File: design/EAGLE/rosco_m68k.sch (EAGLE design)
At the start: 57 parts, among them IC1 74LS04N, IC10 74LS32N, IC11 NE555N, IC12 74LS01N, IC2 MC68010P10, IC3 ATF16V8QL-15PU, IC4 74LS93N, IC5 74S20N, IC6 MC68901P, IC7 74LS08N, IC8 74LS08N, IC9 74LS174N, Q1 1.8432MHz, Q2 8MHz, U1 AT28C64B-15PU, U2 AT28C64B-15PU, U3 AS6C4008-55PCN, U4 AS6C4008-55PCN

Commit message: Cleanup ready for PCB design
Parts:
- added C16, C20, C21, C22, C23, C25, C27, C29: 100nF, capacitor-wima:C2,5-3
- added C17, C18, C19, C28, C30: 100uF, rcl:CPOL-EUE2.5-5
- added C24, C26: 22pF, capacitor-wima:C2,5-3
- added C31: 400uF, rcl:CPOL-EUE3.5-10
- added JP2: PWR, pinhead:PINHD-1X2
- C1, C2: device capacitor-wima:C2.5/2 -> capacitor-wima:C2,5-3
- C10, C7, C8, C9: device capacitor-wima:C5/3 -> capacitor-wima:C2,5-3
- C11: value 22pF -> 33pF; device rcl:C-EU025-025X050 -> capacitor-wima:C2,5-3
- C12: value 100nF -> 33pF; device rcl:C-EU025-025X050 -> capacitor-wima:C2,5-3
- C13: value 22pF -> 100nF; device rcl:C-EU025-025X050 -> capacitor-wima:C2,5-3
- C14: value 100uF -> 100nF; device rcl:CPOL-EUE1.8-4 -> capacitor-wima:C2,5-3
- C3: value 33pF -> 100uF; device capacitor-wima:C2,5-3 -> rcl:CPOL-EUE2.5-5
- C4: value 33pF -> 100nF
- C5: value 100nF -> 100uF; device capacitor-wima:C2,5-3 -> rcl:CPOL-EUE2.5-5
- R1, R10, R11, R12, R5, R6, R7, R8, R9: device rcl:R-US_0207/10 -> rcl:R-EU_0207/10
- R13, R14, R15, R16, R17, R18, R2, R3, R4: device rcl:R-US_0204/7 -> rcl:R-EU_0207/10
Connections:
- net GND: now also C12.2, C14.2, C15.2, C16.2, C17.-, C18.-, C19.-, C20.2, C21.2, C22.2, C23.2, C24.2, C26.2, C27.2, C28.-, C3.-, C30.-, C31.-, C5.-, IC12P.GND, IC1P.GND, IC4P.GND, IC5P.GND, IC8P.GND, JP2.2; no longer C14.-, C3.2, C5.2
- net N$19: now also C29.2; no longer C15.2
- net N$3: now also C25.1; no longer C12.1
- net N$37: now also C28.+; no longer C14.+
- net N$4: now also C25.2; no longer C12.2
- net N$5: now also C26.1; no longer C13.1
- net N$6: now also C24.1; no longer C11.1
- net N$7: now also C11.1; no longer C3.1
- net N$8: now also C12.1; no longer C4.1
- net VCC: now also C13.1, C14.1, C16.1, C17.+, C18.+, C19.+, C20.1, C21.1, C22.1, C23.1, C27.1, C29.1, C3.+, C30.+, C31.+, C4.1, C5.+, IC12P.VCC, IC1P.VCC, IC4P.VCC, IC5P.VCC, IC8P.VCC, JP2.1; no longer C5.1
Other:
- note added: "CLOCK & RESET"
- moved on the sheet: C1, C2, IC10P, IC7P, IC9P

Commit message: Use new PLD glue logic and tidy up
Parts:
- removed C29: 100nF, capacitor-wima:C2,5-3
- removed C30: 100uF, rcl:CPOL-EUE2.5-5
- removed C31: 400uF, rcl:CPOL-EUE3.5-10
- removed IC10: 74LS32N, 74xx-eu:74LS32N
- removed IC11: NE555N, linear:NE555N
- removed IC12: 74LS01N, 74xx-eu:74LS01N
- removed R18: 4K7, rcl:R-EU_0207/10
- added JP3: (no value), pinhead:PINHD-2X30
- added JP4: (no value), pinhead:PINHD-2X2
- C10: value 100nF -> 33pF
- C12: value 33pF -> 100nF
- C16, C2, C25, C27, C4: value 100nF -> 100uF; device capacitor-wima:C2,5-3 -> rcl:CPOL-EUE2.5-5
- C19, C3, C5: value 100uF -> 100nF; device rcl:CPOL-EUE2.5-5 -> capacitor-wima:C2,5-3
- C20, C22: value 100nF -> 22pF
- C24, C26: value 22pF -> 100nF
- C28: value 100uF -> 400uF; device rcl:CPOL-EUE2.5-5 -> rcl:CPOL-EUE3.5-10
- IC1: value 74LS04N -> MC68010P10; device 74xx-eu:74LS04N -> micro-mc68000:MC68000P
- IC2: value MC68010P10 -> ATF16V8QL-15PU; device micro-mc68000:MC68000P -> atmel:ATF16V8BP3; MPN (none) -> ATF16V8QL-15PU; PROG (none) -> ADDRESS_DECODER.PLD
- IC3: value ATF16V8QL-15PU -> 74LS93N; device atmel:ATF16V8BP3 -> 74xx-eu:74LS93N; MPN ATF16V8QL-15PU -> (none); PROG ADDRESS_DECODER.PLD -> (none)
- IC4: value 74LS93N -> MC68901P; device 74xx-eu:74LS93N -> micro-mc68000:MC68901P
- IC5: value 74S20N -> ATF16V8QL-15PU; device 74xx-eu:74S20N -> atmel:ATF16V8BP3; MPN (none) -> ATF16V8QL-15PU; PROG (none) -> GLUE_LOGIC.PLD
- IC6: value MC68901P -> 74LS174N; device micro-mc68000:MC68901P -> 74xx-eu:74LS174N
- IC7: value 74LS08N -> 74LS04N; device 74xx-eu:74LS08N -> 74xx-eu:74LS04N
- IC8: value 74LS08N -> NE555N; device 74xx-eu:74LS08N -> linear:NE555N
- IC9: value 74LS174N -> 74LS01N; device 74xx-eu:74LS174N -> 74xx-eu:74LS01N
- JP1: device pinhead:PINHD-1X3 -> pinhead:PINHD-1X4; 1 CP2102 TXD -> GND; 2 CP2102 RXD -> TXD; 3 CP2102 CTS -> RXD; 4 (none) -> CTS
- R10, R5: value 4K7 -> 1K2
- R11, R6: value 1K2 -> 4K7
- R12: value 4K7 -> 2K2
- R13: value 2K2 -> 270R
- R14: value 270R -> 330R
- R16: value 330R -> 4K7
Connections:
- removed net IACK: IC10B.I1, IC1E.O
- removed net N$11: IC6G$1.RC, IC6G$1.TC, IC6G$1.TDO
- removed net N$12: IC6G$1.I0, LED1.C
- removed net N$13: IC6G$1.SI, JP1.1
- removed net N$14: IC6G$1.SO, JP1.2
- removed net N$15: IC8B.O, IC8C.I0
- removed net N$17: IC6G$1.I1, LED2.C
- removed net N$18: IC6G$1.I7, JP1.3
- removed net N$2: IC2G$1.VPA, R1.1
- removed net N$24: IC8A.O, IC8C.I1
- removed net N$25: IC10B.I0, IC8C.O
- removed net N$27: IC10A.I0, IC8D.O
- removed net N$28: IC10B.O, IC7B.I0
- removed net N$29: IC10A.O, IC7B.I1
- removed net N$7: C11.1, IC6G$1.XTAL1, Q1.1
- removed net N$8: C12.1, IC6G$1.XTAL2, Q1.2
- new net MFPIO0: IC4G$1.I0, LED1.C
- new net MFPIO1: IC4G$1.I1, LED2.C
- new net MFPXTAL1: C10.1, IC4G$1.XTAL1, Q1.1
- new net MFPXTAL2: C11.1, IC4G$1.XTAL2, Q1.2
- new net UARTCLK: IC4G$1.RC, IC4G$1.TC, IC4G$1.TDO
- new net UARTCTS: IC4G$1.I7, JP1.4
- new net UARTRX: IC4G$1.SI, JP1.3
- new net UARTTX: IC4G$1.SO, JP1.2
- new net VPA: IC1G$1.VPA, R1.1
- net /BOOT: now also IC2.I8, IC6A.Q6; no longer IC3.I8, IC9A.Q6
- net /HALT: now also IC1G$1.HALT, IC9A.O, IC9C.I0, IC9C.I1, R16.1; no longer IC12A.O, IC12C.I0, IC12C.I1, IC2G$1.HALT, R17.1
- net /IACK: now also IC2.O2, IC4G$1.IACK, IC5.O7; no longer IC1E.I, IC3.O2, IC5A.O, IC6G$1.IACK, IC7A.I1, IC8D.I0
- net /IODTACK: now also IC4G$1.DTACK, IC5.I8; no longer IC10A.I1, IC6G$1.DTACK, R4.1
- net /MFPDS: now also IC4G$1.DS, IC5.O5; no longer IC6G$1.DS, IC7A.O
- net /RAMOE: now also IC5.O4; no longer IC1A.O
- net A1: now also IC1G$1.A1, IC4G$1.RS5, JP3.1; no longer IC2G$1.A1, IC6G$1.RS5
- net A10: now also IC1G$1.A10, JP3.19; no longer IC2G$1.A10
- net A11: now also IC1G$1.A11, JP3.21; no longer IC2G$1.A11
- net A12: now also IC1G$1.A12, JP3.23; no longer IC2G$1.A12
- net A13: now also IC1G$1.A13, JP3.25; no longer IC2G$1.A13
- net A14: now also IC1G$1.A14, JP3.27; no longer IC2G$1.A14
- net A15: now also IC1G$1.A15, JP3.29; no longer IC2G$1.A15
- net A16: now also IC1G$1.A16, JP3.31; no longer IC2G$1.A16
- net A17: now also IC1G$1.A17, JP3.33; no longer IC2G$1.A17
- net A18: now also IC1G$1.A18, IC2.CLK, JP3.35; no longer IC2G$1.A18, IC3.CLK
- net A19: now also IC1G$1.A19, IC2.I1, JP3.37; no longer IC2G$1.A19, IC3.I1
- net A2: now also IC1G$1.A2, IC4G$1.RS4, JP3.3; no longer IC2G$1.A2, IC6G$1.RS4
- net A20: now also IC1G$1.A20, IC2.I2, JP3.39; no longer IC2G$1.A20, IC3.I2
- net A21: now also IC1G$1.A21, IC2.I3, JP3.41; no longer IC2G$1.A21, IC3.I3
- net A22: now also IC1G$1.A22, IC2.I4, JP3.43; no longer IC2G$1.A22, IC3.I4
- net A23: now also IC1G$1.A23, IC2.I5, JP3.45; no longer IC2G$1.A23, IC3.I5
- net A3: now also IC1G$1.A3, IC4G$1.RS3, JP3.5; no longer IC2G$1.A3, IC6G$1.RS3
- net A4: now also IC1G$1.A4, IC4G$1.RS2, JP3.7; no longer IC2G$1.A4, IC6G$1.RS2
- net A5: now also IC1G$1.A5, IC4G$1.RS1, JP3.9; no longer IC2G$1.A5, IC6G$1.RS1
- net A6: now also IC1G$1.A6, JP3.11; no longer IC2G$1.A6
- net A7: now also IC1G$1.A7, JP3.13; no longer IC2G$1.A7
- net A8: now also IC1G$1.A8, JP3.15; no longer IC2G$1.A8
- net A9: now also IC1G$1.A9, JP3.17; no longer IC2G$1.A9
- net AS: now also IC1G$1.AS, IC2.OE, IC6A.CLK, JP3.47; no longer IC2G$1.AS, IC3.OE, IC9A.CLK
- net BERR: now also IC1G$1.BERR, JP3.49, R11.1; no longer IC2G$1.BERR, R12.1
- net BG: now also IC1G$1.BG, JP3.51; no longer IC2G$1.BG
- net BGACK: now also IC1G$1.BGACK, JP3.53, R9.1; no longer IC2G$1.BGACK, R10.1
- net BR: now also IC1G$1.BR, JP3.55, R8.1; no longer IC2G$1.BR, R9.1
- net CLK: now also IC1G$1.CLK, IC3A.CKA, IC7C.O, JP3.4; no longer IC1D.O, IC2G$1.CLK, IC4A.CKA
- net D0: now also IC1G$1.D0, IC4G$1.D0, JP4.1; no longer IC2G$1.D0, IC6G$1.D0
- net D1: now also IC1G$1.D1, IC4G$1.D1, JP4.3; no longer IC2G$1.D1, IC6G$1.D1
- net D10: now also IC1G$1.D10, JP3.48; no longer IC2G$1.D10
- net D11: now also IC1G$1.D11, JP3.46; no longer IC2G$1.D11
- net D12: now also IC1G$1.D12, JP3.44; no longer IC2G$1.D12
- net D13: now also IC1G$1.D13, JP3.42; no longer IC2G$1.D13
- net D14: now also IC1G$1.D14, JP3.40; no longer IC2G$1.D14
- net D15: now also IC1G$1.D15, JP3.38; no longer IC2G$1.D15
- net D2: now also IC1G$1.D2, IC4G$1.D2, JP4.4; no longer IC2G$1.D2, IC6G$1.D2
- net D3: now also IC1G$1.D3, IC4G$1.D3, JP4.2; no longer IC2G$1.D3, IC6G$1.D3
- net D4: now also IC1G$1.D4, IC4G$1.D4, JP3.60; no longer IC2G$1.D4, IC6G$1.D4
- net D5: now also IC1G$1.D5, IC4G$1.D5, JP3.58; no longer IC2G$1.D5, IC6G$1.D5
- net D6: now also IC1G$1.D6, IC4G$1.D6, JP3.56; no longer IC2G$1.D6, IC6G$1.D6
- net D7: now also IC1G$1.D7, IC4G$1.D7, JP3.54; no longer IC2G$1.D7, IC6G$1.D7
- net D8: now also IC1G$1.D8, JP3.52; no longer IC2G$1.D8
- net D9: now also IC1G$1.D9, JP3.50; no longer IC2G$1.D9
- net DTACK: now also IC1G$1.DTACK, IC5.O6, JP3.57; no longer IC2G$1.DTACK, IC7B.O
- net EVENRAMSEL: now also IC2.O8, IC5.I6, JP3.8; no longer IC3.O8, IC8A.I1
- net EVENROMSEL: now also IC2.O6, IC5.I5, JP3.10; no longer IC3.O6, IC8B.I1
- net EXPSEL: now also IC2.O3, JP3.18; no longer IC3.O3
- net FC0: now also IC1G$1.FC0, IC5.CLK, JP3.20; no longer IC2G$1.FC0, IC5A.I3
- net FC1: now also IC1G$1.FC1, IC5.I1, JP3.22; no longer IC2G$1.FC1, IC5A.I2
- net FC2: now also IC1G$1.FC2, IC5.I2, JP3.24; no longer IC2G$1.FC2, IC5A.I0, IC5A.I1
- net GND: now also C16.-, C19.2, C2.-, C25.-, C27.-, C3.2, C4.-, C5.2, IC1P.GND@1, IC1P.GND@2, IC2.GND, IC3A.CKB, IC3A.R0(1), IC3A.R0(2), IC3P.GND, IC4G$1.IEI, IC4G$1.TAI, IC4G$1.TBI, IC5.GND, IC5.OE, IC6A.D2, IC6A.D5, IC7D.I, IC7E.I, IC7F.I, IC8.GND, IC9D.I0, IC9D.I1, JP1.1, JP3.6, R13.1; no longer C16.2, C19.-, C2.2, C21.2, C26.2, C27.2, C3.-, C30.-, C31.-, C4.2, C5.-, IC10C.I0, IC10C.I1, IC10D.I0, IC10D.I1, IC10P.GND, IC11.GND, IC12D.I0, IC12D.I1, IC12P.GND, IC1F.I, IC1P.GND, IC2P.GND@1, IC2P.GND@2, IC3.GND, IC4A.CKB, IC4A.R0(1), IC4A.R0(2), IC5B.I0, IC5B.I1, IC5B.I2, IC5B.I3, IC5P.GND, IC6G$1.IEI, IC6G$1.TAI, IC6G$1.TBI, IC7C.I0, IC7C.I1, IC7D.I0, IC7D.I1, IC8P.GND, IC9A.D2, IC9A.D5, R15.1
- net IOSEL: now also IC2.O4, IC4G$1.CS, IC5.I7, JP3.16; no longer IC3.O4, IC6G$1.CS, IC8D.I1
- net IPL0: now also IC1G$1.IPL0, JP3.26, R7.1; no longer IC2G$1.IPL0, R8.1
- net IPL1: now also IC1G$1.IPL1, JP3.28, R6.1; no longer IC2G$1.IPL1, R7.1
- net IPL2: now also IC1G$1.IPL2, IC4G$1.IRQ, JP3.30, R4.1; no longer IC2G$1.IPL2, IC6G$1.IRQ, R5.1
- net LDS: now also IC1G$1.LDS, IC2.I7, IC5.O2, JP3.32; no longer IC2G$1.LDS, IC3.I7, IC7A.I0
- net MFPCLK: now also IC3A.QA, IC4G$1.CLK; no longer IC4A.QA, IC6G$1.CLK
- net N$16: now also IC6A.D4, IC6A.Q3; no longer IC9A.D4, IC9A.Q3
- net N$19: now also C26.2, IC8.CV; no longer C29.2, IC11.CV
- net N$20: now also R14.2; no longer R15.2
- net N$22: now also IC6A.D6, IC6A.Q4; no longer IC9A.D6, IC9A.Q4
- net N$23: now also IC6A.D3, IC6A.Q1; no longer IC9A.D3, IC9A.Q1
- net N$3: now also C21.1, IC7A.O, R5.2; no longer C25.1, IC1B.O, R6.2
- net N$33: now also IC9C.O; no longer IC12C.O
- net N$34: now also R15.1; no longer R16.1
- net N$35: now also IC8.Q, IC9A.I0, IC9A.I1, IC9B.I0, IC9B.I1; no longer IC11.Q, IC12A.I0, IC12A.I1, IC12B.I0, IC12B.I1
- net N$36: now also R13.2; no longer R14.2
- net N$37: now also C25.+, IC8.THR, IC8.TR, R12.1; no longer C28.+, IC11.THR, IC11.TR, R13.1
- net N$4: now also C21.2, IC7B.I, R10.1; no longer C25.2, IC1C.I, R11.1
- net N$5: now also C22.1, IC7B.O, IC7C.I, R10.2; no longer C26.1, IC1C.O, IC1D.I, R11.2
- net N$6: now also C20.1, IC7A.I, R5.1; no longer C24.1, IC1B.I, R6.1
- net ODDRAMSEL: now also IC2.O7, IC5.I4, JP3.12; no longer IC3.O7, IC8A.I0
- net ODDROMSEL: now also IC2.O5, IC5.I3, JP3.14; no longer IC3.O5, IC8B.I0
- net R/W: now also IC1G$1.R/W, IC4G$1.R/!W, IC5.O3, JP3.59; no longer IC1A.I, IC2G$1.R/W, IC6G$1.R/!W
- net RESET: now also IC1G$1.RESET, IC4G$1.RESET, IC6A.CLR, IC9B.O, JP3.36, R17.1; no longer IC12B.O, IC2G$1.RESET, IC6G$1.RESET, IC9A.CLR, R18.1
- net UDS: now also IC1G$1.UDS, IC2.I6, JP3.34; no longer IC2G$1.UDS, IC3.I6
- net VCC: now also C12.1, C16.+, C19.1, C2.+, C24.1, C26.1, C27.+, C28.+, C3.1, C4.+, C5.1, IC1P.VCC@1, IC1P.VCC@2, IC2.VCC, IC3P.VCC, IC5.VCC, IC6A.D1, IC8.R, IC8.V+, JP3.2, R11.2, R15.2, R6.2; no longer C10.1, C16.1, C19.+, C2.1, C20.1, C21.1, C22.1, C27.1, C29.1, C3.+, C30.+, C31.+, C4.1, C5.+, IC10P.VCC, IC11.R, IC11.V+, IC12P.VCC, IC1P.VCC, IC2P.VCC@1, IC2P.VCC@2, IC3.VCC, IC5P.VCC, IC8P.VCC, IC9A.D1, R10.2, R13.2, R18.2, R5.2
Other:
- note added: "EXPANSION"
- note removed: "/DTACK GENERATOR"
- note removed: "O/E Generator for RAM"

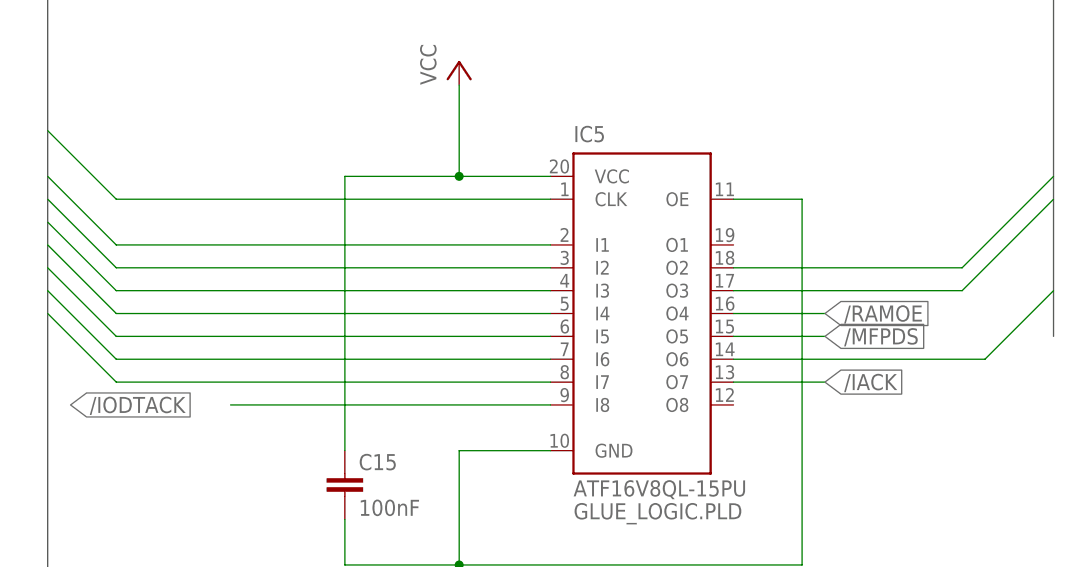
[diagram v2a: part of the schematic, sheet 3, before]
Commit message: Fix misplaced capacitor
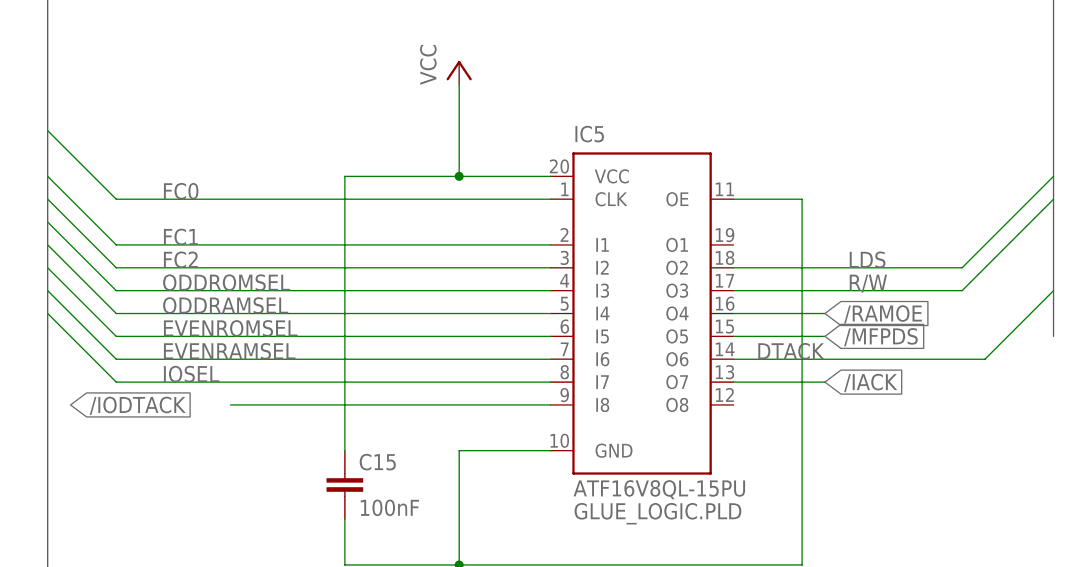
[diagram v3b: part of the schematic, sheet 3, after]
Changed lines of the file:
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@@
 <pinref part="IC5" gate="G$1" pin="CLK"/>
 <wire x1="-33.02" y1="116.84" x2="15.24" y2="116.84" width="0.1524" layer="91"/>
+<label x="-27.94" y="116.84" size="1.778" layer="95"/>
 </segment>
 </net>
@@
 <pinref part="IC5" gate="G$1" pin="I1"/>
 <wire x1="-33.02" y1="111.76" x2="15.24" y2="111.76" width="0.1524" layer="91"/>
+<label x="-27.94" y="111.76" size="1.778" layer="95"/>
 </segment>
 </net>
@@
 <pinref part="IC5" gate="G$1" pin="I2"/>
 <wire x1="-33.02" y1="109.22" x2="15.24" y2="109.22" width="0.1524" layer="91"/>
+<label x="-27.94" y="109.22" size="1.778" layer="95"/>
 </segment>
 </net>
@@
 <pinref part="IC5" gate="G$1" pin="I3"/>
 <wire x1="-33.02" y1="106.68" x2="15.24" y2="106.68" width="0.1524" layer="91"/>
+<label x="-27.94" y="106.68" size="1.778" layer="95"/>
 </segment>
 </net>
@@
 <pinref part="IC5" gate="G$1" pin="I4"/>
 <wire x1="-33.02" y1="104.14" x2="15.24" y2="104.14" width="0.1524" layer="91"/>
+<label x="-27.94" y="104.14" size="1.778" layer="95"/>
 </segment>
 </net>
@@
 <pinref part="IC5" gate="G$1" pin="I5"/>
 <wire x1="-33.02" y1="101.6" x2="15.24" y2="101.6" width="0.1524" layer="91"/>
+<label x="-27.94" y="101.6" size="1.778" layer="95"/>
 </segment>
 </net>
@@
 <pinref part="IC5" gate="G$1" pin="I6"/>
 <wire x1="-33.02" y1="99.06" x2="15.24" y2="99.06" width="0.1524" layer="91"/>
+<label x="-27.94" y="99.06" size="1.778" layer="95"/>
 </segment>
 </net>
@@
 <pinref part="IC5" gate="G$1" pin="I7"/>
 <wire x1="-33.02" y1="96.52" x2="15.24" y2="96.52" width="0.1524" layer="91"/>
+<label x="-27.94" y="96.52" size="1.778" layer="95"/>
 </segment>
 </net>
@@
 <pinref part="IC5" gate="G$1" pin="O6"/>
 <wire x1="63.5" y1="99.06" x2="35.56" y2="99.06" width="0.1524" layer="91"/>
+<label x="38.1" y="99.06" size="1.778" layer="95"/>
 </segment>
 </net>
@@
 <pinref part="IC5" gate="G$1" pin="O3"/>
 <wire x1="60.96" y1="106.68" x2="35.56" y2="106.68" width="0.1524" layer="91"/>
+<label x="48.26" y="106.68" size="1.778" layer="95"/>
 </segment>
 </net>
@@
 <pinref part="IC5" gate="G$1" pin="O2"/>
 <wire x1="60.96" y1="109.22" x2="35.56" y2="109.22" width="0.1524" layer="91"/>
+<label x="48.26" y="109.22" size="1.778" layer="95"/>
 </segment>
 </net>
